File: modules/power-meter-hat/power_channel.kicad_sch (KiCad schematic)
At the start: 8 parts, among them J5 Conn_01x02, U5 INA219AxD

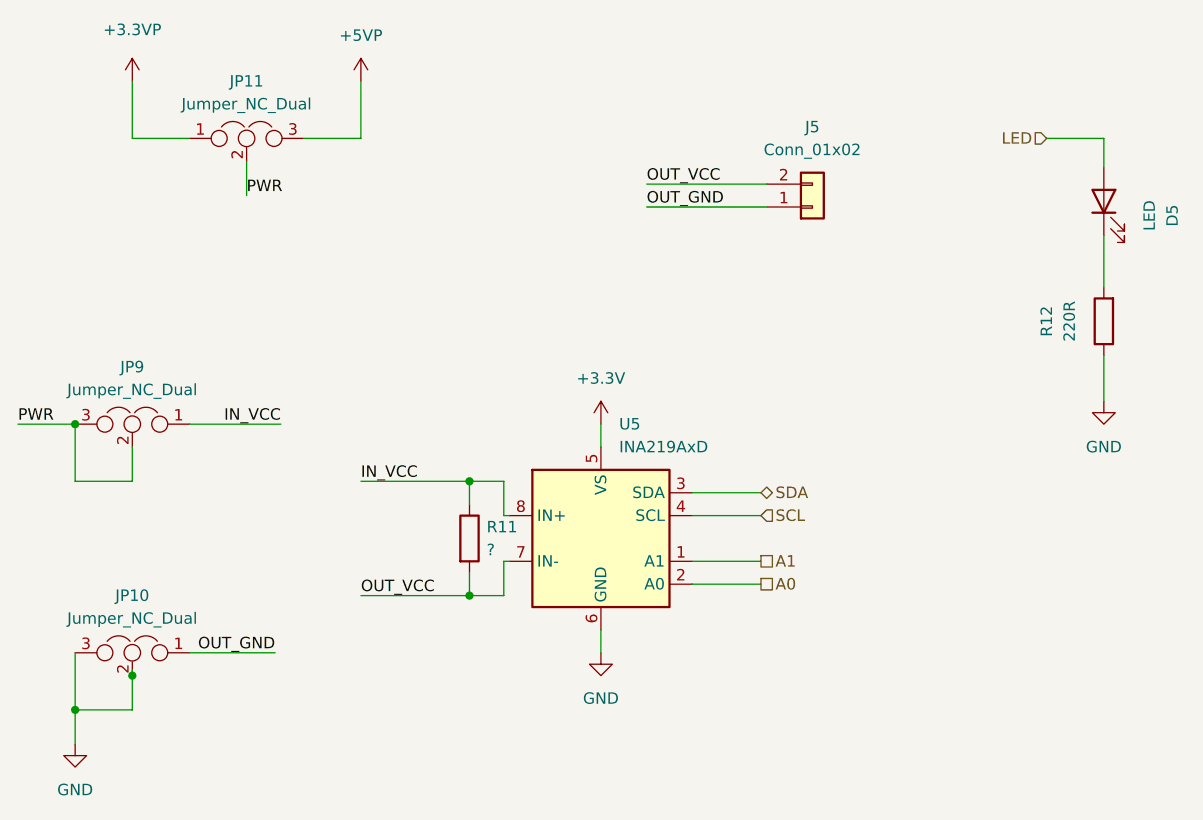
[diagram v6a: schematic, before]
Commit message: Update components and footprints
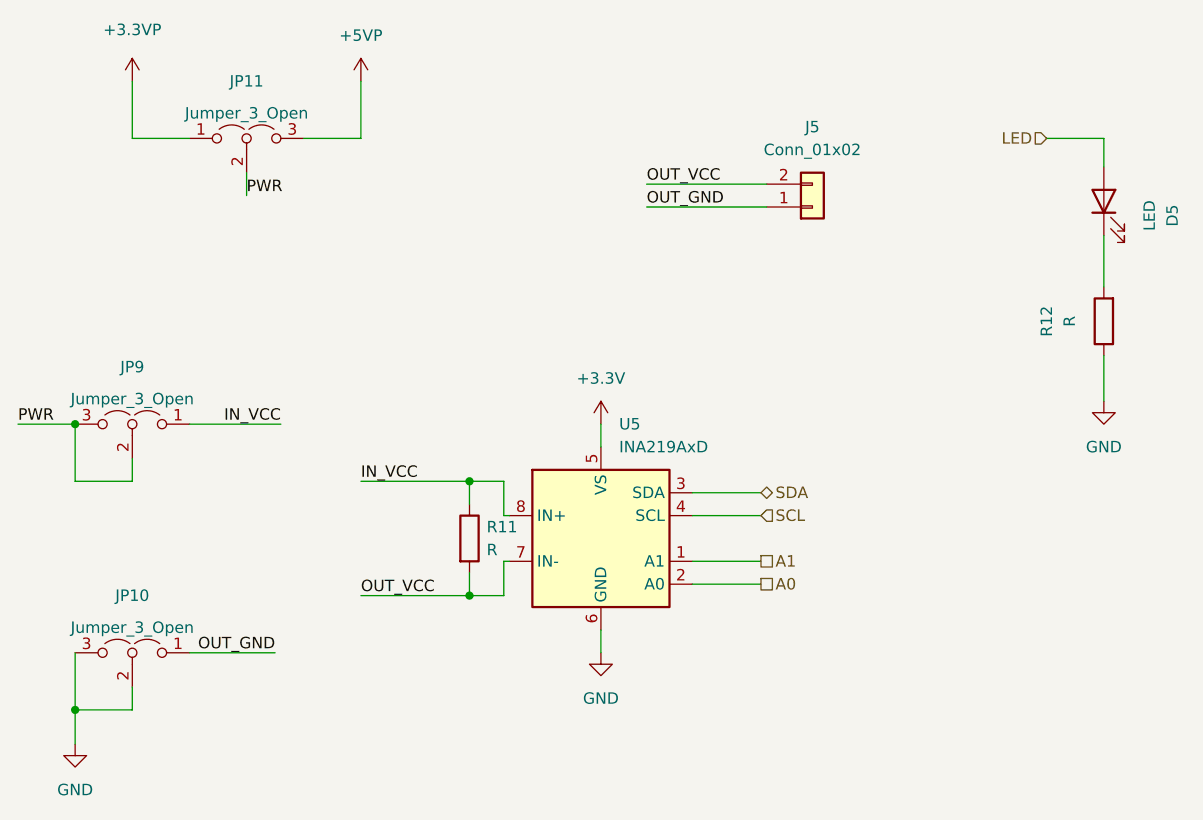
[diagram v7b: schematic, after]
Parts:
- D5: footprint LED_SMD:LED_1206_3216Metric_Castellated -> LED_SMD:LED_1206_3216Metric
- JP10, JP11, JP9: value Jumper_NC_Dual -> Jumper_3_Open; symbol Device:Jumper_NC_Dual -> Jumper:Jumper_3_Open
- R11: value ? -> R
- R12: value 220R -> R
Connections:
- net +3V3 renamed +3.3V
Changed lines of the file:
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@@
   (junction (at 69.85 63.5) (diameter 0) (color 0 0 0 0)
   )
-  (junction (at 76.2 91.44) (diameter 0) (color 0 0 0 0)
-  )
   (junction (at 113.665 69.85) (diameter 0) (color 0 0 0 0)
   )
@@
     (stroke (width 0) (type default) (color 0 0 0 0))
   )
+  (wire (pts (xy 88.9 35.56) (xy 88.9 38.1))
+    (stroke (width 0) (type default) (color 0 0 0 0))
+  )
   (wire (pts (xy 69.85 95.25) (xy 69.85 99.06))
     (stroke (width 0) (type default) (color 0 0 0 0))
@@
     (stroke (width 0) (type default) (color 0 0 0 0))
   )
-  (wire (pts (xy 76.2 95.25) (xy 76.2 91.44))
-    (stroke (width 0) (type default) (color 0 0 0 0))
-  )
   (wire (pts (xy 101.6 69.85) (xy 113.665 69.85))
     (stroke (width 0) (type default) (color 0 0 0 0))
@@
     (stroke (width 0) (type default) (color 0 0 0 0))
   )
-  (wire (pts (xy 76.2 91.44) (xy 76.2 90.805))
-    (stroke (width 0) (type default) (color 0 0 0 0))
-  )
-  (wire (pts (xy 88.9 34.29) (xy 88.9 38.1))
-    (stroke (width 0) (type default) (color 0 0 0 0))
-  )
   (wire (pts (xy 138.43 78.74) (xy 146.05 78.74))
     (stroke (width 0) (type default) (color 0 0 0 0))
   )
-  (wire (pts (xy 76.2 66.04) (xy 76.2 69.85))
-    (stroke (width 0) (type default) (color 0 0 0 0))
-  )
   (wire (pts (xy 133.35 39.37) (xy 146.685 39.37))
+    (stroke (width 0) (type default) (color 0 0 0 0))
+  )
+  (wire (pts (xy 76.2 67.31) (xy 76.2 69.85))
+    (stroke (width 0) (type default) (color 0 0 0 0))
+  )
+  (wire (pts (xy 76.2 92.71) (xy 76.2 95.25))
     (stroke (width 0) (type default) (color 0 0 0 0))
   )
@@
     (effects (font (size 1.27 1.27)) (justify left))
   )
-  (symbol (lib_id "Device:Jumper_NC_Dual") (at 76.2 63.5 0) (mirror y)
+  (symbol (lib_id "Jumper:Jumper_3_Open") (at 76.2 63.5 0) (mirror y)
     (in_bom yes) (on_board yes) (fields_autoplaced)
     (property "Reference" "JP9" (id 0) (at 76.2 57.15 0))
-    (property "Value" "Jumper_NC_Dual" (id 1) (at 76.2 59.69 0))
+    (property "Value" "Jumper_3_Open" (id 1) (at 76.2 60.706 0))
     (property "Footprint" "Connector_PinHeader_2.54mm:PinHeader_1x03_P2.54mm_Vertical" (id 2) (at 76.2 63.5 0)
       (effects (font (size 1.27 1.27)) hide)
@@
       (effects (font (size 1.27 1.27)) (justify left))
     )
-    (property "Value" "?" (id 1) (at 115.57 77.4699 0)
+    (property "Value" "R" (id 1) (at 115.57 77.4699 0)
       (effects (font (size 1.27 1.27)) (justify left))
     )
@@
     (in_bom yes) (on_board yes) (fields_autoplaced)
     (property "Reference" "R12" (id 0) (at 177.8 52.07 90))
-    (property "Value" "220R" (id 1) (at 180.34 52.07 90))
+    (property "Value" "R" (id 1) (at 180.34 52.07 90))
     (property "Footprint" "Resistor_SMD:R_0805_2012Metric_Pad1.20x1.40mm_HandSolder" (id 2) (at 185.928 52.07 90)
       (effects (font (size 1.27 1.27)) hide)
@@
     (pin "1")
   )
-  (symbol (lib_id "Device:Jumper_NC_Dual") (at 88.9 31.75 0)
+  (symbol (lib_id "Jumper:Jumper_3_Open") (at 88.9 31.75 0)
     (in_bom yes) (on_board yes) (fields_autoplaced)
     (property "Reference" "JP11" (id 0) (at 88.9 25.4 0))
-    (property "Value" "Jumper_NC_Dual" (id 1) (at 88.9 27.94 0))
+    (property "Value" "Jumper_3_Open" (id 1) (at 88.9 28.956 0))
     (property "Footprint" "Connector_PinHeader_2.54mm:PinHeader_1x03_P2.54mm_Vertical" (id 2) (at 88.9 31.75 0)
       (effects (font (size 1.27 1.27)) hide)
@@
     (pin "3")
   )
-  (symbol (lib_id "Device:Jumper_NC_Dual") (at 76.2 88.9 0) (mirror y)
+  (symbol (lib_id "Jumper:Jumper_3_Open") (at 76.2 88.9 0) (mirror y)
     (in_bom yes) (on_board yes) (fields_autoplaced)
     (property "Reference" "JP10" (id 0) (at 76.2 82.55 0))
-    (property "Value" "Jumper_NC_Dual" (id 1) (at 76.2 85.09 0))
+    (property "Value" "Jumper_3_Open" (id 1) (at 76.2 86.106 0))
     (property "Footprint" "Connector_PinHeader_2.54mm:PinHeader_1x03_P2.54mm_Vertical" (id 2) (at 76.2 88.9 0)
       (effects (font (size 1.27 1.27)) hide)
@@
     (property "Reference" "D5" (id 0) (at 191.77 40.3225 0))
     (property "Value" "LED" (id 1) (at 189.23 40.3225 0))
-    (property "Footprint" "LED_SMD:LED_1206_3216Metric_Castellated" (id 2) (at 184.15 38.735 0)
-      (effects (font (size 1.27 1.27)) hide)
-    )
+    (property "Footprint" "LED_SMD:LED_1206_3216Metric" (id 2) (at 184.15 38.735 0)
+      (effects (font (size 1.27 1.27)) hide)
+    )

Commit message: Add "ideal diode" and fuse, update values
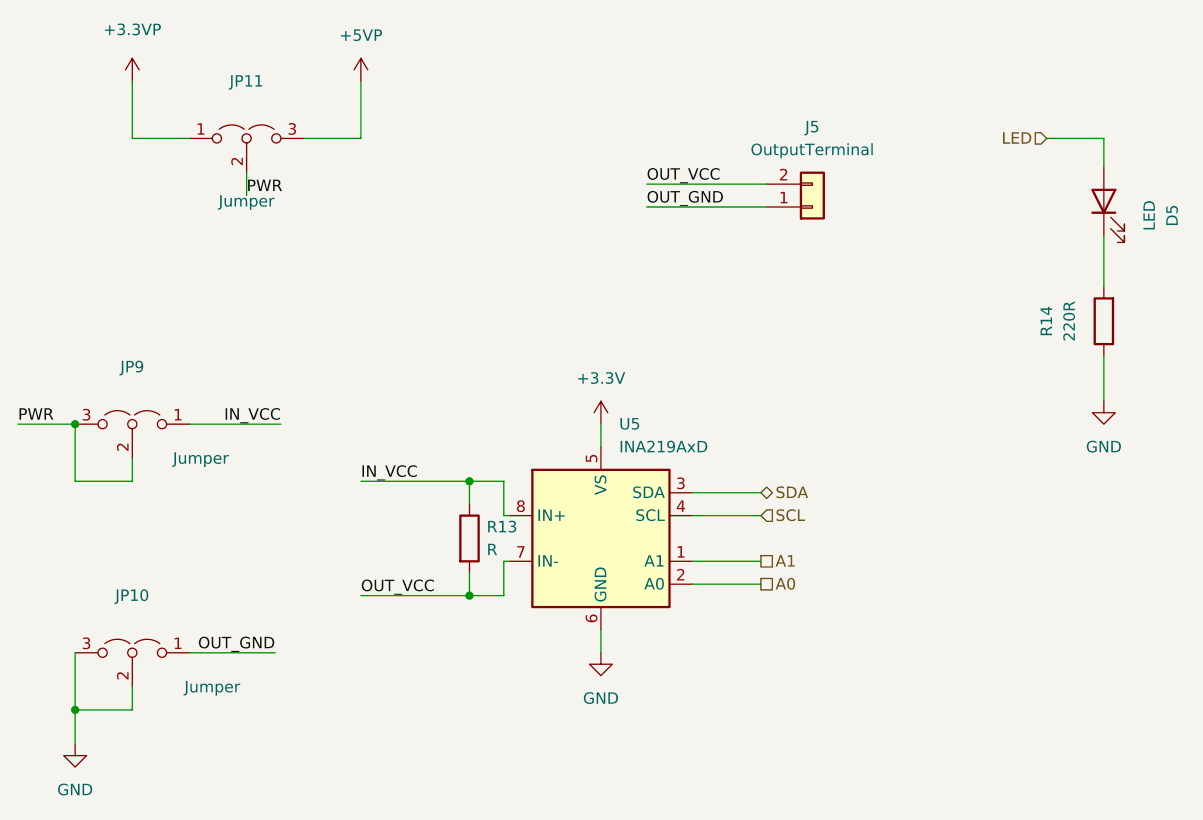
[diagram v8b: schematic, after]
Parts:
- J5: value Conn_01x02 -> OutputTerminal
- JP10, JP11, JP9: value Jumper_3_Open -> Jumper
- R14: renamed from R12; value R -> 220R
- renumbered R11 to R13
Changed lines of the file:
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@@
   )
   (symbol (lib_id "Jumper:Jumper_3_Open") (at 76.2 63.5 0) (mirror y)
-    (in_bom yes) (on_board yes) (fields_autoplaced)
+    (in_bom yes) (on_board yes)
     (property "Reference" "JP9" (id 0) (at 76.2 57.15 0))
-    (property "Value" "Jumper_3_Open" (id 1) (at 76.2 60.706 0))
+    (property "Value" "Jumper" (id 1) (at 83.82 67.31 0))
     (property "Footprint" "Connector_PinHeader_2.54mm:PinHeader_1x03_P2.54mm_Vertical" (id 2) (at 76.2 63.5 0)
       (effects (font (size 1.27 1.27)) hide)
@@
   (symbol (lib_id "power:+3.3V") (at 128.27 63.5 0)
     (in_bom yes) (on_board yes) (fields_autoplaced)
-    (property "Reference" "#PWR037" (id 0) (at 128.27 67.31 0)
+    (property "Reference" "#PWR040" (id 0) (at 128.27 67.31 0)
       (effects (font (size 1.27 1.27)) hide)
     )
@@
   (symbol (lib_id "Device:R") (at 113.665 76.2 0)
     (in_bom yes) (on_board yes) (fields_autoplaced)
-    (property "Reference" "R11" (id 0) (at 115.57 74.9299 0)
+    (property "Reference" "R13" (id 0) (at 115.57 74.9299 0)
       (effects (font (size 1.27 1.27)) (justify left))
     )
@@
   (symbol (lib_id "Device:R") (at 184.15 52.07 180)
     (in_bom yes) (on_board yes) (fields_autoplaced)
-    (property "Reference" "R12" (id 0) (at 177.8 52.07 90))
-    (property "Value" "R" (id 1) (at 180.34 52.07 90))
+    (property "Reference" "R14" (id 0) (at 177.8 52.07 90))
+    (property "Value" "220R" (id 1) (at 180.34 52.07 90))
     (property "Footprint" "Resistor_SMD:R_0805_2012Metric_Pad1.20x1.40mm_HandSolder" (id 2) (at 185.928 52.07 90)
       (effects (font (size 1.27 1.27)) hide)
@@
   (symbol (lib_id "power:GND") (at 69.85 99.06 0)
     (in_bom yes) (on_board yes) (fields_autoplaced)
-    (property "Reference" "#PWR034" (id 0) (at 69.85 105.41 0)
+    (property "Reference" "#PWR037" (id 0) (at 69.85 105.41 0)
       (effects (font (size 1.27 1.27)) hide)
     )
@@
     (in_bom yes) (on_board yes) (fields_autoplaced)
     (property "Reference" "J5" (id 0) (at 151.765 30.48 0))
-    (property "Value" "Conn_01x02" (id 1) (at 151.765 33.02 0))
+    (property "Value" "OutputTerminal" (id 1) (at 151.765 33.02 0))
     (property "Footprint" "TerminalBlock_Phoenix:TerminalBlock_Phoenix_PT-1,5-2-3.5-H_1x02_P3.50mm_Horizontal" (id 2) (at 151.765 39.37 0)
       (effects (font (size 1.27 1.27)) hide)
@@
   (symbol (lib_id "power:GND") (at 184.15 60.96 0)
     (in_bom yes) (on_board yes) (fields_autoplaced)
-    (property "Reference" "#PWR039" (id 0) (at 184.15 67.31 0)
+    (property "Reference" "#PWR042" (id 0) (at 184.15 67.31 0)
       (effects (font (size 1.27 1.27)) hide)
     )
@@
   )
   (symbol (lib_id "Jumper:Jumper_3_Open") (at 88.9 31.75 0)
-    (in_bom yes) (on_board yes) (fields_autoplaced)
+    (in_bom yes) (on_board yes)
     (property "Reference" "JP11" (id 0) (at 88.9 25.4 0))
-    (property "Value" "Jumper_3_Open" (id 1) (at 88.9 28.956 0))
+    (property "Value" "Jumper" (id 1) (at 88.9 38.735 0))
     (property "Footprint" "Connector_PinHeader_2.54mm:PinHeader_1x03_P2.54mm_Vertical" (id 2) (at 88.9 31.75 0)
       (effects (font (size 1.27 1.27)) hide)
@@
   )
   (symbol (lib_id "Jumper:Jumper_3_Open") (at 76.2 88.9 0) (mirror y)
-    (in_bom yes) (on_board yes) (fields_autoplaced)
+    (in_bom yes) (on_board yes)
     (property "Reference" "JP10" (id 0) (at 76.2 82.55 0))
-    (property "Value" "Jumper_3_Open" (id 1) (at 76.2 86.106 0))
+    (property "Value" "Jumper" (id 1) (at 85.09 92.71 0))
     (property "Footprint" "Connector_PinHeader_2.54mm:PinHeader_1x03_P2.54mm_Vertical" (id 2) (at 76.2 88.9 0)
       (effects (font (size 1.27 1.27)) hide)
@@
   (symbol (lib_id "power:+3.3VP") (at 76.2 25.4 0)
     (in_bom yes) (on_board yes) (fields_autoplaced)
-    (property "Reference" "#PWR035" (id 0) (at 80.01 26.67 0)
+    (property "Reference" "#PWR038" (id 0) (at 80.01 26.67 0)
       (effects (font (size 1.27 1.27)) hide)
     )
@@
   (symbol (lib_id "power:+5VP") (at 101.6 25.4 0)
     (in_bom yes) (on_board yes) (fields_autoplaced)
-    (property "Reference" "#PWR036" (id 0) (at 101.6 29.21 0)
+    (property "Reference" "#PWR039" (id 0) (at 101.6 29.21 0)
       (effects (font (size 1.27 1.27)) hide)
     )
@@
   (symbol (lib_id "power:GND") (at 128.27 88.9 0)
     (in_bom yes) (on_board yes) (fields_autoplaced)
-    (property "Reference" "#PWR038" (id 0) (at 128.27 95.25 0)
+    (property "Reference" "#PWR041" (id 0) (at 128.27 95.25 0)
       (effects (font (size 1.27 1.27)) hide)
     )
